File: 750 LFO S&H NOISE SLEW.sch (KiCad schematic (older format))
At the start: 237 parts, among them J1 JACK_MONO_SW, J10 JACK_MONO_SW, J11 JACK_MONO_SW, J2 JACK_MONO_SW, J3 JACK_MONO_SW, J4 JACK_MONO_SW, J5 JACK_MONO_SW, J6 JACK_MONO_SW, J7 JACK_MONO_SW, J8 JACK_MONO_SW, J9 JACK_MONO_SW, P1 CONN_02X01, P2 CONN_02X01, P3 CONN_02X05, Q1 MMBT3904, Q10 MMBT3904, Q11 J112, Q12 MMBT3906, Q13 J112, Q14 J112, Q15 MMBT3904, Q16 MMBT3904, Q2 MMBT3904, Q3 2N7002, Q4 2N7002, Q5 MBT3946DW, Q6 DMMT3904W, Q7 MMBT3904, Q8 MMBT3904, Q9 MMBT3904, SW1 KS-01Q, SW2 KS-01Q, U1 LM13700, U10 TL072-, U11 TL072-, U12 MAX9945, U13 DG409, U14 DG409, U2 TL072-, U3 TL072-, U4 TL072-, U5 TL072-, U6 CD40106, U7 CD4027, U8 CD4027, U9 TL072-

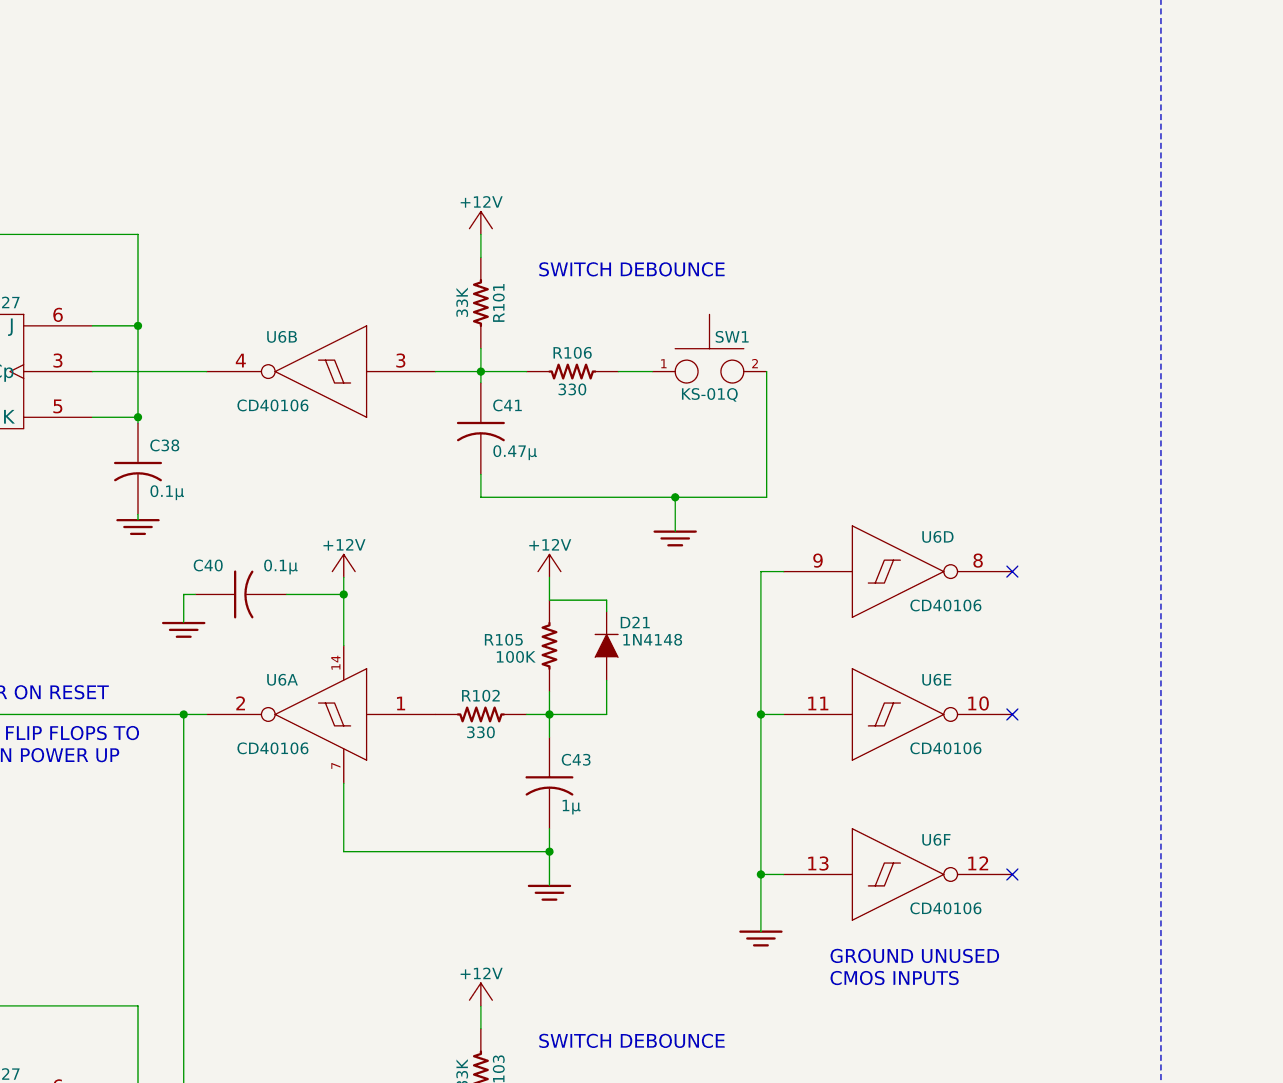
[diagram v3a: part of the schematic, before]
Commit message: everything placed but some test points and all decoupling caps
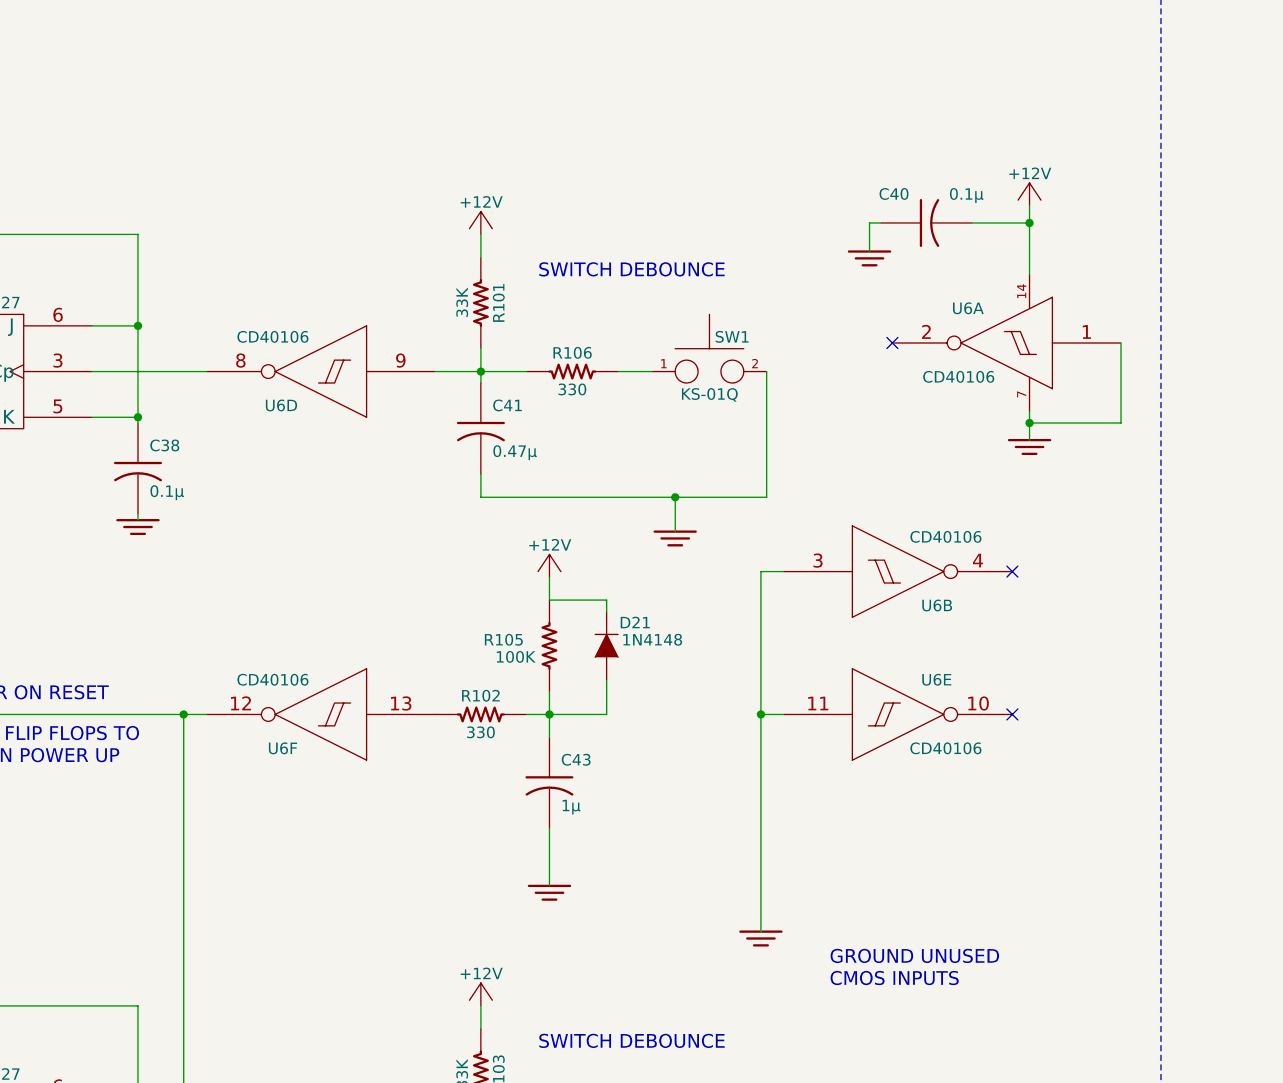
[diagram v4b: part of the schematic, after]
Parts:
- C34: footprint MyModules:2MM-POL-CAP -> MyModules:SM0805-HAND
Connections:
- net GND: now also U6.1 (In), U6.3 (In); no longer U6.13 (In), U6.9 (In)
- net at C41.1, R101.1, R106.1: now also U6.9 (In); no longer U6.3 (In)
- net at U7.3 (Cp): now also U6.8 (Out); no longer U6.4 (Out)
- net at U7.12 (Cd), U7.4 (Cd), U8.12 (Cd)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: now also U6.12 (Out); no longer U6.2 (Out)
- net at R102.1: now also U6.13 (In); no longer U6.1 (In)
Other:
- moved on the sheet: C40, U6A, U6B, U6D, U6F
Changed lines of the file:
@@
 F 0 "C34" H 11275 4575 50  0000 L CNN
 F 1 "4.7μ" H 11275 4375 50  0000 L CNN
-F 2 "MyModules:2MM-POL-CAP" H 11225 4475 60  0001 C CNN
+F 2 "MyModules:SM0805-HAND" H 11225 4475 60  0001 C CNN
 F 3 "" H 11225 4475 60  0000 C CNN
 	1    11225 4475
@@
 L +12V #PWR055
 U 1 1 56EECA3B
-P 24400 9850
-F 0 "#PWR055" H 24400 9700 50  0001 C CNN
-F 1 "+12V" H 24400 9990 50  0000 C CNN
-F 2 "" H 24400 9850 60  0000 C CNN
-F 3 "" H 24400 9850 60  0000 C CNN
-	1    24400 9850
+P 27400 8225
+F 0 "#PWR055" H 27400 8075 50  0001 C CNN
+F 1 "+12V" H 27400 8365 50  0000 C CNN
+F 2 "" H 27400 8225 60  0000 C CNN
+F 3 "" H 27400 8225 60  0000 C CNN
+	1    27400 8225
 	-1   0    0    -1
 $EndComp
@@
 L CD40106 U6
 U 2 1 56EECA46
-P 24300 8950
-F 0 "U6" H 24400 9100 50  0000 L CNN
-F 1 "CD40106" H 24350 8800 50  0000 L CNN
-F 2 "Housings_SSOP:TSSOP-14_4.4x5mm_Pitch0.65mm" H 24300 8950 60  0001 C CNN
-F 3 "" H 24300 8950 60  0000 C CNN
-	2    24300 8950
-	-1   0    0    -1
+P 26825 9825
+F 0 "U6" H 26925 9975 50  0000 L CNN
+F 1 "CD40106" H 26875 9675 50  0000 L CNN
+F 2 "Housings_SSOP:TSSOP-14_4.4x5mm_Pitch0.65mm" H 26825 9825 60  0001 C CNN
+F 3 "" H 26825 9825 60  0000 C CNN
+	2    26825 9825
+	1    0    0    1
 $EndComp
 $Comp
 L CD40106 U6
 U 1 1 56EECA47
-P 24300 10450
-F 0 "U6" H 24400 10600 50  0000 L CNN
-F 1 "CD40106" H 24350 10300 50  0000 L CNN
-F 2 "Housings_SSOP:TSSOP-14_4.4x5mm_Pitch0.65mm" H 24300 10450 60  0001 C CNN
-F 3 "" H 24300 10450 60  0000 C CNN
-	1    24300 10450
+P 27300 8825
+F 0 "U6" H 27400 8975 50  0000 L CNN
+F 1 "CD40106" H 27350 8675 50  0000 L CNN
+F 2 "Housings_SSOP:TSSOP-14_4.4x5mm_Pitch0.65mm" H 27300 8825 60  0001 C CNN
+F 3 "" H 27300 8825 60  0000 C CNN
+	1    27300 8825
 	-1   0    0    -1
 $EndComp
@@
 $EndComp
 NoConn ~ 27325 10450
-NoConn ~ 27325 11150
 Wire Wire Line
 	17750 8300 17600 8300
@@
 	19325 7950 22100 7950
 Wire Wire Line
-	24400 9850 24400 10150
+	27400 8225 27400 8525
 Wire Wire Line
 	24800 8950 25200 8950
@@
 $EndComp
 Wire Wire Line
-	24400 10750 24400 11050
-Wire Wire Line
-	24400 11050 25300 11050
-Connection ~ 25300 11050
-Wire Wire Line
 	25000 9500 26250 9500
 Text Notes 22050 7925 0    60   ~ 0
@@
 L CD40106 U6
 U 6 1 56EECA4A
-P 26825 11150
-F 0 "U6" H 26925 11300 50  0000 L CNN
-F 1 "CD40106" H 26875 11000 50  0000 L CNN
-F 2 "Housings_SSOP:TSSOP-14_4.4x5mm_Pitch0.65mm" H 26825 11150 60  0001 C CNN
-F 3 "" H 26825 11150 60  0000 C CNN
-	6    26825 11150
-	1    0    0    -1
+P 24300 10450
+F 0 "U6" H 24400 10600 50  0000 L CNN
+F 1 "CD40106" H 24350 10300 50  0000 L CNN
+F 2 "Housings_SSOP:TSSOP-14_4.4x5mm_Pitch0.65mm" H 24300 10450 60  0001 C CNN
+F 3 "" H 24300 10450 60  0000 C CNN
+	6    24300 10450
+	-1   0    0    1
 $EndComp
 $Comp
@@
 	26225 9825 26225 11400
 Wire Wire Line
-	26325 11150 26225 11150
-Connection ~ 26225 11150
-Wire Wire Line
 	20075 8050 19325 8050
 $Comp
@@
 L CD40106 U6
 U 4 1 56F12D88
-P 26825 9825
-F 0 "U6" H 26925 9975 50  0000 L CNN
-F 1 "CD40106" H 26875 9675 50  0000 L CNN
-F 2 "Housings_SSOP:TSSOP-14_4.4x5mm_Pitch0.65mm" H 26825 9825 60  0001 C CNN
-F 3 "" H 26825 9825 60  0000 C CNN
-	4    26825 9825
-	1    0    0    -1
+P 24300 8950
+F 0 "U6" H 24400 9100 50  0000 L CNN
+F 1 "CD40106" H 24350 8800 50  0000 L CNN
+F 2 "Housings_SSOP:TSSOP-14_4.4x5mm_Pitch0.65mm" H 24300 8950 60  0001 C CNN
+F 3 "" H 24300 8950 60  0000 C CNN
+	4    24300 8950
+	-1   0    0    1
 $EndComp
 Wire Wire Line
@@
 L C_US C40
 U 1 1 56F68273
-P 23950 9925
-F 0 "C40" V 23825 10000 50  0000 L CNN
-F 1 "0.1µ" V 23825 9675 50  0000 L CNN
-F 2 "MyModules:SM0603-C-JRL" H 23950 9925 60  0001 C CNN
-F 3 "~" H 23950 9925 60  0000 C CNN
-	1    23950 9925
+P 26950 8300
+F 0 "C40" V 26825 8375 50  0000 L CNN
+F 1 "0.1µ" V 26825 8050 50  0000 L CNN
+F 2 "MyModules:SM0603-C-JRL" H 26950 8300 60  0001 C CNN
+F 3 "~" H 26950 8300 60  0000 C CNN
+	1    26950 8300
 	0    -1   1    0
 $EndComp
@@
 L GND_E #PWR0146
 U 1 1 56F6C2BF
-P 23700 10050
-F 0 "#PWR0146" V 23700 10050 30  0001 C CNN
-F 1 "GND_E" H 23700 9980 30  0001 C CNN
-F 2 "" H 23700 10050 60  0000 C CNN
-F 3 "" H 23700 10050 60  0000 C CNN
-	1    23700 10050
+P 26700 8425
+F 0 "#PWR0146" V 26700 8425 30  0001 C CNN
+F 1 "GND_E" H 26700 8355 30  0001 C CNN
+F 2 "" H 26700 8425 60  0000 C CNN
+F 3 "" H 26700 8425 60  0000 C CNN
+	1    26700 8425
 	1    0    0    -1
 $EndComp
 Wire Wire Line
-	24150 9925 24400 9925
-Connection ~ 24400 9925
+	27150 8300 27400 8300
+Connection ~ 27400 8300
 Wire Wire Line
-	23750 9925 23700 9925
+	26750 8300 26700 8300
 Wire Wire Line
-	23700 9925 23700 10050
+	26700 8300 26700 8425
 Text Notes 2975 2175 0    60   ~ 0
 NOISE \nLEVEL
@@
 Wire Notes Line
 	27850 3250 27850 3775
+$Comp
+L GND_E #PWR?
+U 1 1 570C8DBC
+P 27400 9250
+F 0 "#PWR?" V 27400 9250 30  0001 C CNN
+F 1 "GND_E" H 27400 9180 30  0001 C CNN
+F 2 "" H 27400 9250 60  0000 C CNN
+F 3 "" H 27400 9250 60  0000 C CNN
+	1    27400 9250
+	1    0    0    -1
+$EndComp
+Wire Wire Line
+	27400 9125 27400 9250
+NoConn ~ 26800 8825
+Wire Wire Line
+	27400 9175 27800 9175
+Wire Wire Line
+	27800 9175 27800 8825
+Connection ~ 27400 9175
 $EndSCHEMATC

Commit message: routing power
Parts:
- removed R77: 1K, MyModules:SM0603-R-JRL, symbol R_US
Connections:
- net S&H_TRI is gone; now on net S&H_INT_CLK: J9.2
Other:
- note added: "SECRET S&H SLEW PULSE"
- note removed: "SECRET S&H TRI OUTPUT"
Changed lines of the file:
@@
 	10150 3700 10150 4750
 Wire Wire Line
-	9750 3700 12500 3700
+	9750 3700 12550 3700
 Wire Wire Line
 	9350 3350 8825 3350
@@
 Wire Wire Line
 	15250 3050 15400 3050
-Text Label 12500 3700 0    60   ~ 0
-S&H_INT_CLK
 Wire Wire Line
 	12500 2800 12500 2900
@@
 Text Notes 11625 2800 0    60   ~ 0
 S&H EXT CLK
-Text GLabel 12525 5050 2    50   Output ~ 0
-S&H_TRI
 Text GLabel 17825 7350 0    50   Input ~ 0
 LFO_TRI
@@
 	28050 3125 28425 3125
 Wire Wire Line
-	11775 5050 12100 5050
-Text GLabel 22775 4200 0    50   Input ~ 0
-S&H_TRI
-Wire Wire Line
 	22775 3475 23025 3475
 Wire Wire Line
@@
 Wire Wire Line
 	23025 4200 22775 4200
-Text Notes 22400 4350 0    60   ~ 0
-SECRET S&H TRI OUTPUT
 $Comp
 L GND_E #PWR050
@@
 Connection ~ 10800 10750
 $Comp
-L R_US R77
-U 1 1 56FF4969
-P 12300 5050
-F 0 "R77" V 12380 5050 50  0000 C CNN
-F 1 "1K" V 12220 5050 50  0000 C CNN
-F 2 "MyModules:SM0603-R-JRL" H 12300 5050 60  0001 C CNN
-F 3 "" H 12300 5050 60  0000 C CNN
-	1    12300 5050
-	0    1    1    0
-$EndComp
-Wire Wire Line
-	12525 5050 12500 5050
-$Comp
 L DIODE D8
 U 1 1 56FFBBD3
@@
 	6825 2600 6825 3175
 Connection ~ 6825 3075
-Text GLabel 6925 2700 2    50   Output ~ 0
+Text GLabel 6950 2700 2    50   Output ~ 0
 WHITE_NOISE
-Wire Wire Line
-	6925 2700 6825 2700
 $Comp
 L R_US R20
@@
 	27850 3250 27850 3775
 $Comp
-L GND_E #PWR?
+L GND_E #PWR0165
 U 1 1 570C8DBC
 P 27400 9250
-F 0 "#PWR?" V 27400 9250 30  0001 C CNN
+F 0 "#PWR0165" V 27400 9250 30  0001 C CNN
 F 1 "GND_E" H 27400 9180 30  0001 C CNN
 F 2 "" H 27400 9250 60  0000 C CNN
@@
 	27800 9175 27800 8825
 Connection ~ 27400 9175
+Text Notes 22400 4350 0    60   ~ 0
+SECRET S&H SLEW PULSE
+Text GLabel 12550 3700 2    50   Output ~ 0
+S&H_INT_CLK
+Connection ~ 12500 3700
+Text GLabel 22775 4200 0    50   Input ~ 0
+S&H_INT_CLK
+Wire Wire Line
+	6825 2700 6950 2700
 $EndSCHEMATC
